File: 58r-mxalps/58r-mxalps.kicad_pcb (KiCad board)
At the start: 2 copper layers, 285.5 x 75.8 mm, 242 parts, among them P1 USB_OTG, P2 CONN_01X03, P3 CONN_01X15, P4 CONN_01X04, U1 ATmega32U4, Y1 Crystal_Small

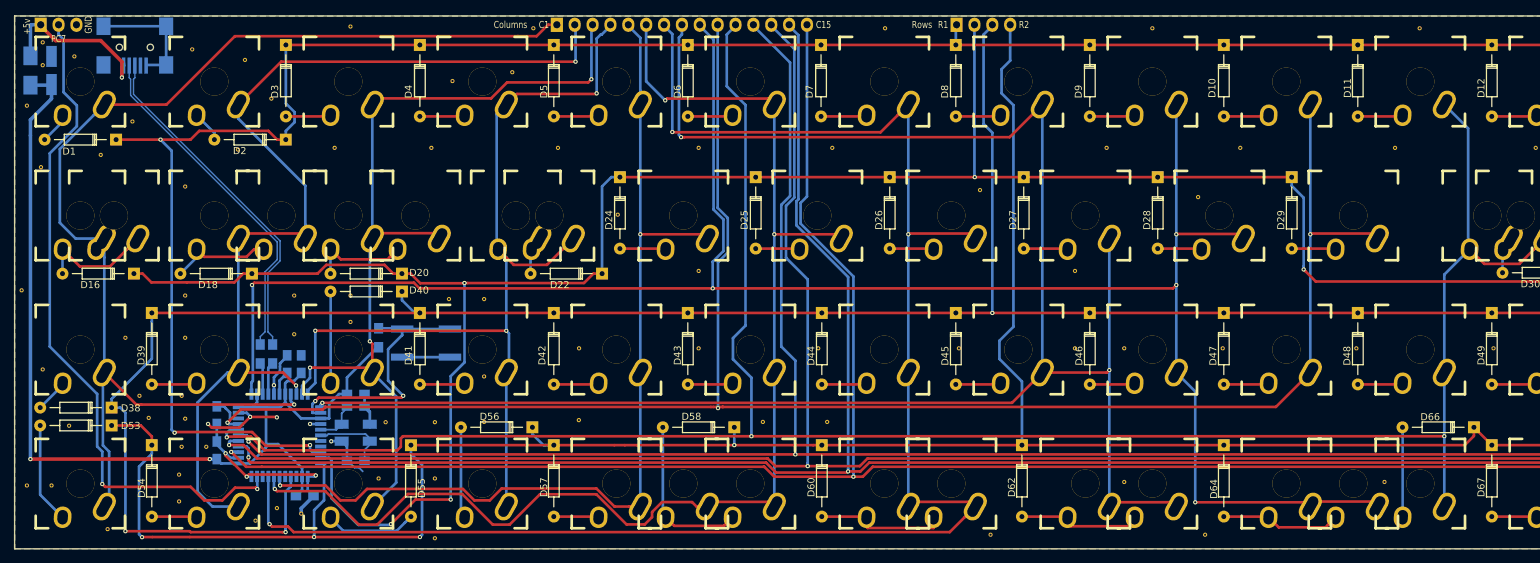
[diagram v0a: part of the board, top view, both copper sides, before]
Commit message: Moved diodes that interfered with stab wire.
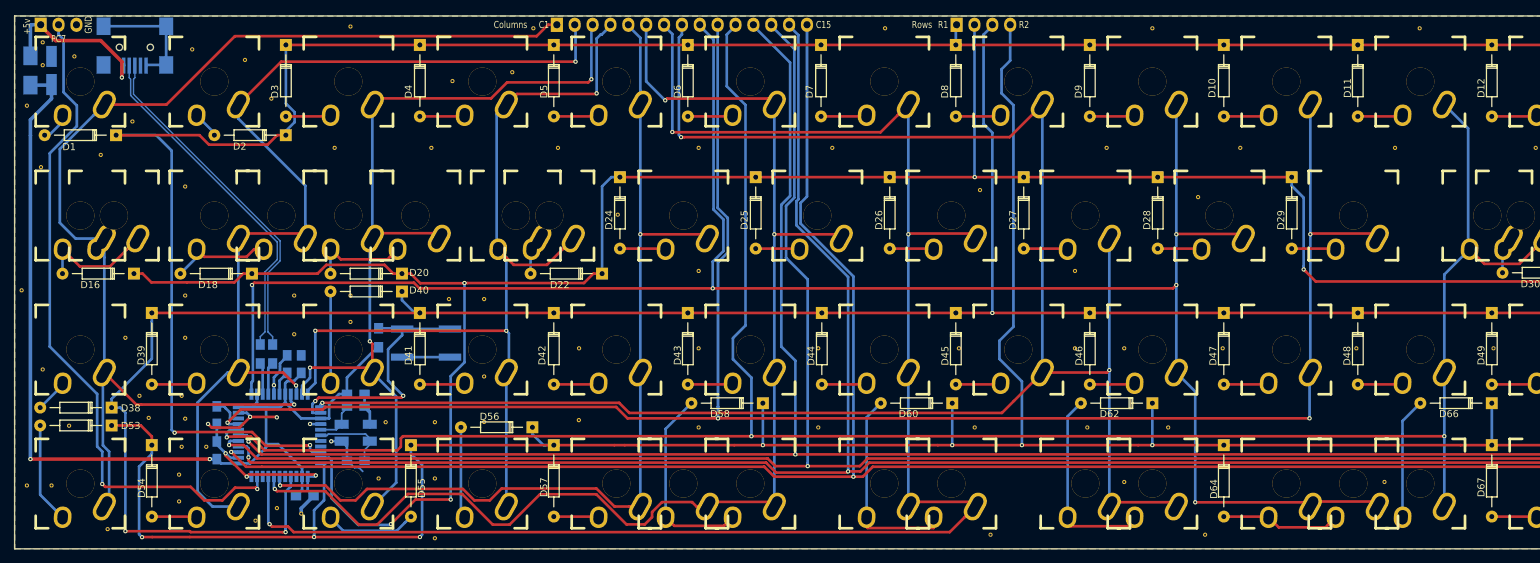
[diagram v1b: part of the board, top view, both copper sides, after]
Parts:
- removed the REF** at (144.3, 77.0)
- removed the REF** at (135.1, 77.0)
- removed the REF** at (60.5, 38.2)
- added REF**: GND Via, Keyboard:GNDVia-wRing, F.Cu at (126.0, 77.8)
- added REF**: GND Via, Keyboard:GNDVia-wRing, F.Cu at (143.0, 77.8)
- added REF**: GND Via, Keyboard:GNDVia-wRing, F.Cu at (165.2, 77.8)
- added REF**: GND Via, Keyboard:GNDVia-wRing, F.Cu at (192.8, 77.8)
- added REF**: GND Via, Keyboard:GNDVia-wRing, F.Cu at (181.2, 77.8)
- moved D62 19.5 mm to (190.5, 74.3), turned to 180 degrees
- moved D60 19.5 mm to (162.1, 74.3), turned to 180 degrees
- moved D58 5.32 mm to (135.1, 74.3)
- moved D66 4.27 mm to (238.8, 74.3)
- moved D1 0.64 mm to (43.2, 36.2)
- moved D2 0.64 mm to (67.3, 36.2)
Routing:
- net R4: track 371.0 -> 389.3 mm, vias 4 -> 7
- net Net-(D62-Pad2): track 18.2 -> 29.0 mm
- net Net-(D60-Pad2): track 18.9 -> 29.7 mm
- net R1: track 336.8 -> 343.5 mm, vias 3 -> 2
- net C10: track 263.1 -> 269.5 mm, vias 3 -> 4
- net Net-(D58-Pad2): track 24.2 -> 29.3 mm
- net Net-(D66-Pad2): track 12.8 -> 17.3 mm
- net C8: track 270.4 -> 271.6 mm
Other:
- net class Default: clearance 0.2032 -> 0.1905
- rule trace_clearance: 0.2032 -> 0.1905

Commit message: LFK78 RevC addedd
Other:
- board text added: "Col 1"
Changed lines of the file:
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@@
     (area 26.472191 14.371 324.6 99.450001)
     (thickness 1.6)
-    (drawings 25)
+    (drawings 35)
     (tracks 1060)
     (zones 0)
@@
   (page A2)
   (layers
-    (0 F.Cu signal hide)
-    (31 B.Cu signal hide)
+    (0 F.Cu signal)
+    (31 B.Cu signal)
     (32 B.Adhes user hide)
     (33 F.Adhes user hide)
@@
     (35 F.Paste user hide)
     (36 B.SilkS user)
-    (37 F.SilkS user)
-    (38 B.Mask user)
-    (39 F.Mask user)
+    (37 F.SilkS user hide)
+    (38 B.Mask user hide)
+    (39 F.Mask user hide)
     (40 Dwgs.User user hide)
-    (41 Cmts.User user)
-    (42 Eco1.User user)
-    (43 Eco2.User user)
+    (41 Cmts.User user hide)
+    (42 Eco1.User user hide)
+    (43 Eco2.User user hide)
     (44 Edge.Cuts user)
     (45 Margin user hide)
@@
     (pad_to_mask_clearance 0.2)
     (aux_axis_origin 0 0)
-    (visible_elements FFFFEF7F)
+    (visible_elements FFFFFF7F)
     (pcbplotparams
       (layerselection 0x010f0_80000001)
@@
     )
   )
+  (gr_text "Col 1" (at 36.068 42.164 360) (layer B.SilkS)
+    (effects (font (size 1 0.8) (thickness 0.2)) (justify mirror))
+  )
+  (gr_line (start 38.1 28.448) (end 38.1 43.18) (layer B.SilkS) (width 0.2))
+  (gr_line (start 40.64 43.688) (end 40.64 43.18) (layer B.SilkS) (width 0.2))
+  (gr_line (start 33.02 85.852) (end 38.1 85.852) (layer B.SilkS) (width 0.2))
+  (gr_line (start 33.02 66.548) (end 33.02 85.852) (layer B.SilkS) (width 0.2))
+  (gr_line (start 33.02 66.548) (end 38.1 66.548) (layer B.SilkS) (width 0.2))
+  (gr_line (start 33.02 43.18) (end 33.02 66.548) (layer B.SilkS) (width 0.2))
+  (gr_line (start 40.64 43.18) (end 33.02 43.18) (layer B.SilkS) (width 0.2))
+  (gr_line (start 40.64 43.434) (end 39.116 45.72) (layer B.SilkS) (width 0.2))
+  (gr_line (start 42.164 45.72) (end 40.64 43.434) (layer B.SilkS) (width 0.2))
   (dimension 75.75 (width 0.3) (layer Cmts.User)
     (gr_text "75.750 mm" (at 318.1 57.125 90) (layer Cmts.User)
